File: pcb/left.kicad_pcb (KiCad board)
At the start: 2 copper layers, 123.5 x 102 mm, 110 parts, among them J2 USB_B_Micro, SW1 SW_Push, SW10 SW_Push, SW11 SW_Push, SW12 SW_Push, SW13 SW_Push, SW14 SW_Push, SW15 SW_Push, SW16 SW_Push, SW17 SW_Push, SW18 SW_Push, SW19 SW_Push, SW2 SW_Push, SW20 SW_Push, SW21 SW_Push, SW22 SW_Push, SW23 SW_Push, SW3 SW_Push, SW4 SW_Push, SW47 SW_Push, SW49 SW_Push, SW5 SW_Push, SW6 SW_Push, SW7 SW_Push, SW8 SW_Push, SW9 SW_Push, U1 ProMicro

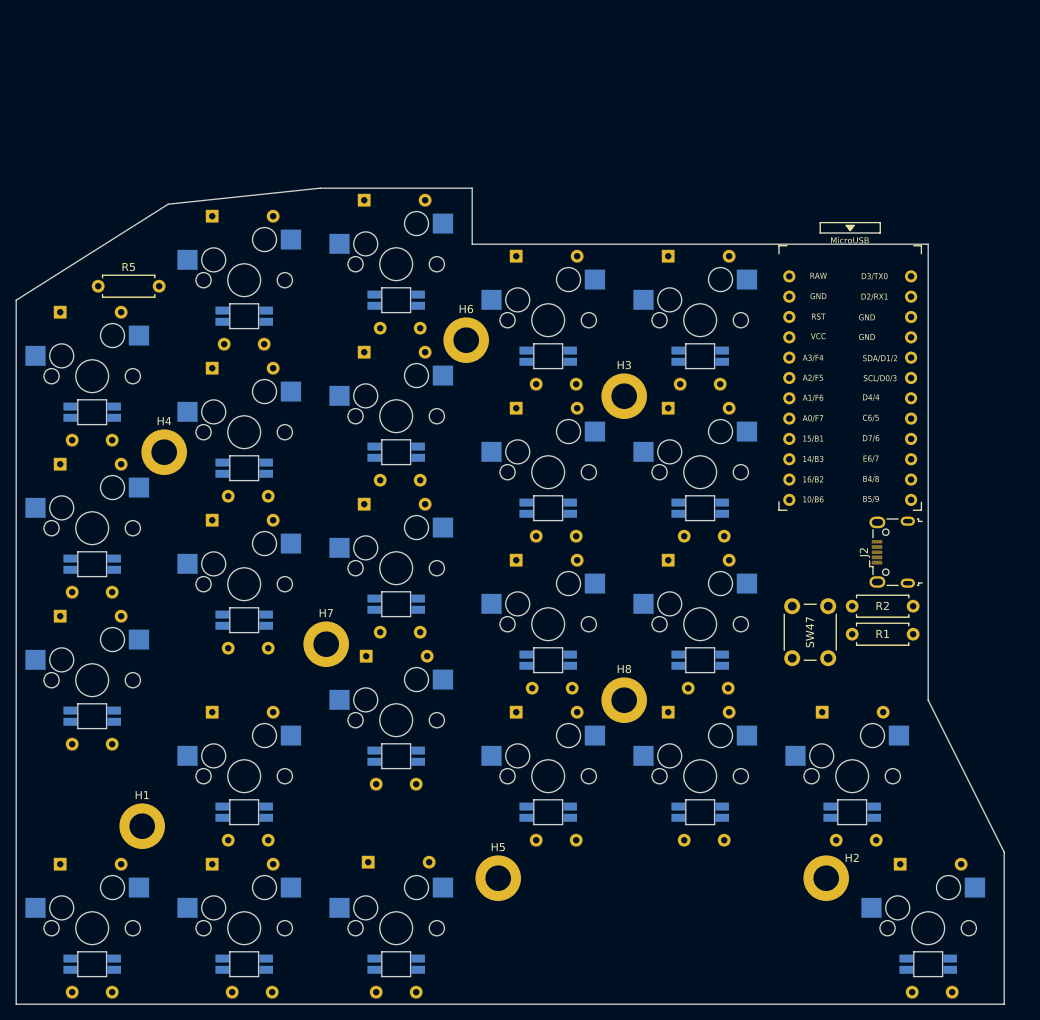
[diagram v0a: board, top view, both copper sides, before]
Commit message: update board rules
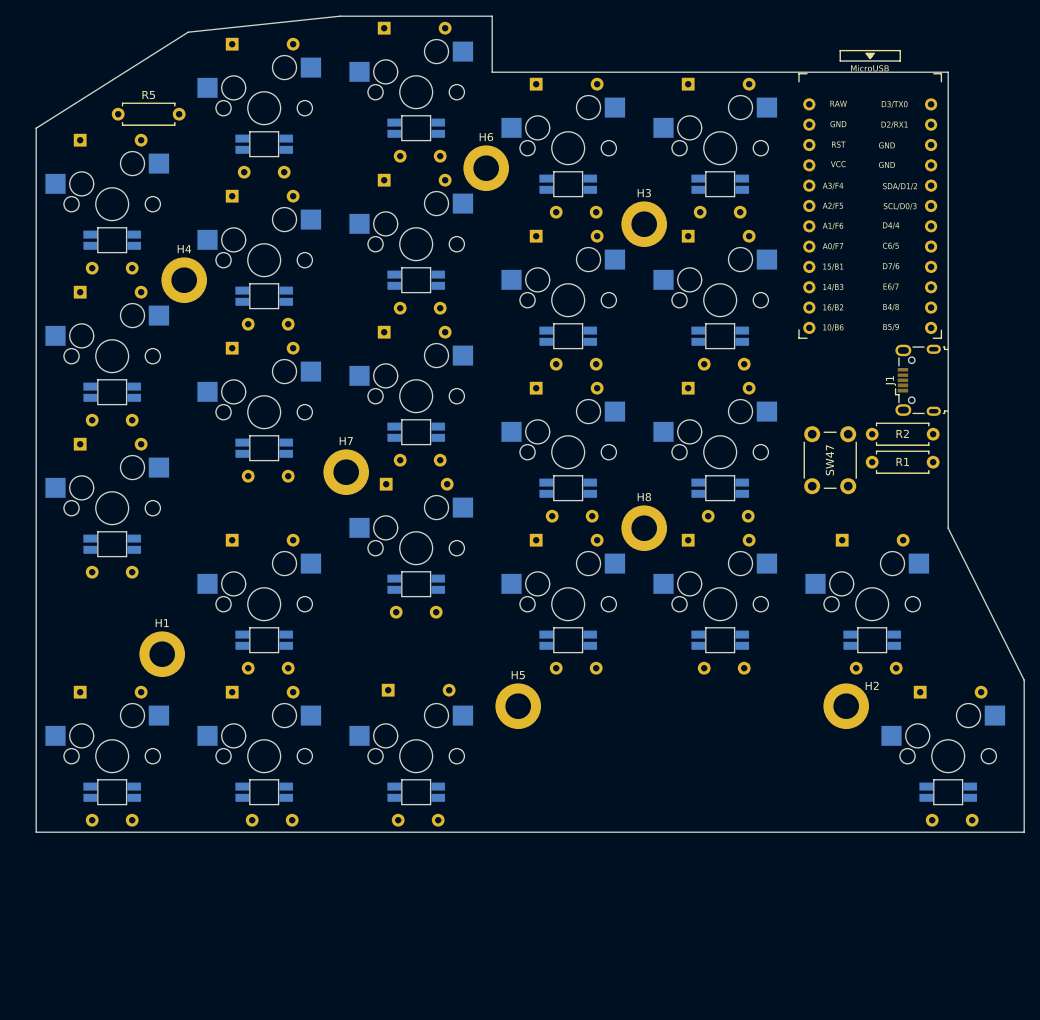
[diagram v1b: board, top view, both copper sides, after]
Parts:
- removed J2: USB_B_Micro, Connector_USB:USB_Micro-B_Wuerth_629105150521
- added J1: USB_B_Micro, Connector_USB:USB_Micro-B_Wuerth_629105150521, F.Cu at (127.7, 60.8)
- moved C1 21.6 mm to (24.5, 46.8)
- moved C10 21.6 mm to (44.0, 96.8)
- moved C11 21.6 mm to (63.0, 32.8)
- moved C12 21.6 mm to (63.0, 51.8)
- moved C13 21.6 mm to (63.0, 70.8)
- moved C14 21.6 mm to (101.0, 96.8)
- moved C15 21.6 mm to (44.5, 115.8)
- moved C16 21.6 mm to (82.5, 39.8)
- moved C17 21.6 mm to (82.5, 58.8)
- moved C18 21.6 mm to (82.0, 77.8)
- moved C19 21.6 mm to (120.0, 96.8)
- moved C2 21.6 mm to (24.5, 65.8)
- moved C20 21.6 mm to (100.5, 39.8)
- moved C21 21.6 mm to (101.0, 58.8)
- moved C22 21.6 mm to (101.5, 77.8)
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
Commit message: update
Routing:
- net +5V: track 0.00 -> 674.6 mm
- net GND: track 0.00 -> 654.4 mm, vias 0 -> 1
- net /lcol2: track 0.00 -> 267.4 mm, vias 0 -> 3
- net /lcol0: track 0.00 -> 210.6 mm, vias 0 -> 2
- net /lcol3: track 0.00 -> 201.4 mm, vias 0 -> 1
- net /lcol4: track 0.00 -> 192.6 mm, vias 0 -> 2
- net /lcol1: track 0.00 -> 179.4 mm, vias 0 -> 2
- net /lrow4: track 0.00 -> 152.4 mm, vias 0 -> 1
- net /lrow3: track 0.00 -> 137.4 mm, vias 0 -> 1
- net /lrow2: track 0.00 -> 117.2 mm
- net Net-(LED23-Pad2): track 0.00 -> 107.4 mm
- net /lrow0: track 0.00 -> 107.1 mm
- net /lrow1: track 0.00 -> 102.9 mm
- net Net-(LED21-Pad2): track 0.00 -> 101.6 mm, vias 0 -> 2
- net /lLED: track 0.00 -> 97.0 mm
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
